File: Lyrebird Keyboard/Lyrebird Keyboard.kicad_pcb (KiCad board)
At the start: 4 copper layers, 220.1 x 160.3 mm, 99 parts, among them IC1 L7915CV, IC2 L78S15CV, IC3 MCP6022-E_SN, IC4 IR2113SPBF, IC5 IR2113SPBF, IC6 LM358DT, IC7 L7805ACD2T-TR, J1 WAV/ENV 4 (MIDI), J10 AC IN 2, J11 240V Out, J12 240 In, J13 Keys 1 to 14, J14 Keys 15 to 28, J15 Keys 29 to 33, J16 Keys 34 to 45, J17 Keys 46 to 59, J18 Keys 60 to 73, J19 Triangle Test, J2 WAV/ENV 3, J20 AMP Out, J21 SUB Out, J22 Square Test, J23 Bias Test Point 2, J24 Bias Test Point 1, J25 Pedals, J3 WAV/ENV 2, J4 WAV/ENV 1, J5 TONE SRC 4, J6 TONE SRC 3, J7 TONE SRC 2, J8 TONE SRC 1, J9 AC IN 1, Q1 BC848, Q2 BC848, Q3 IRFR2905ZTRPBF, Q4 IRFR2905ZTRPBF, Q5 IRFR2905ZTRPBF, Q6 IRFR2905ZTRPBF, U1 DF06S

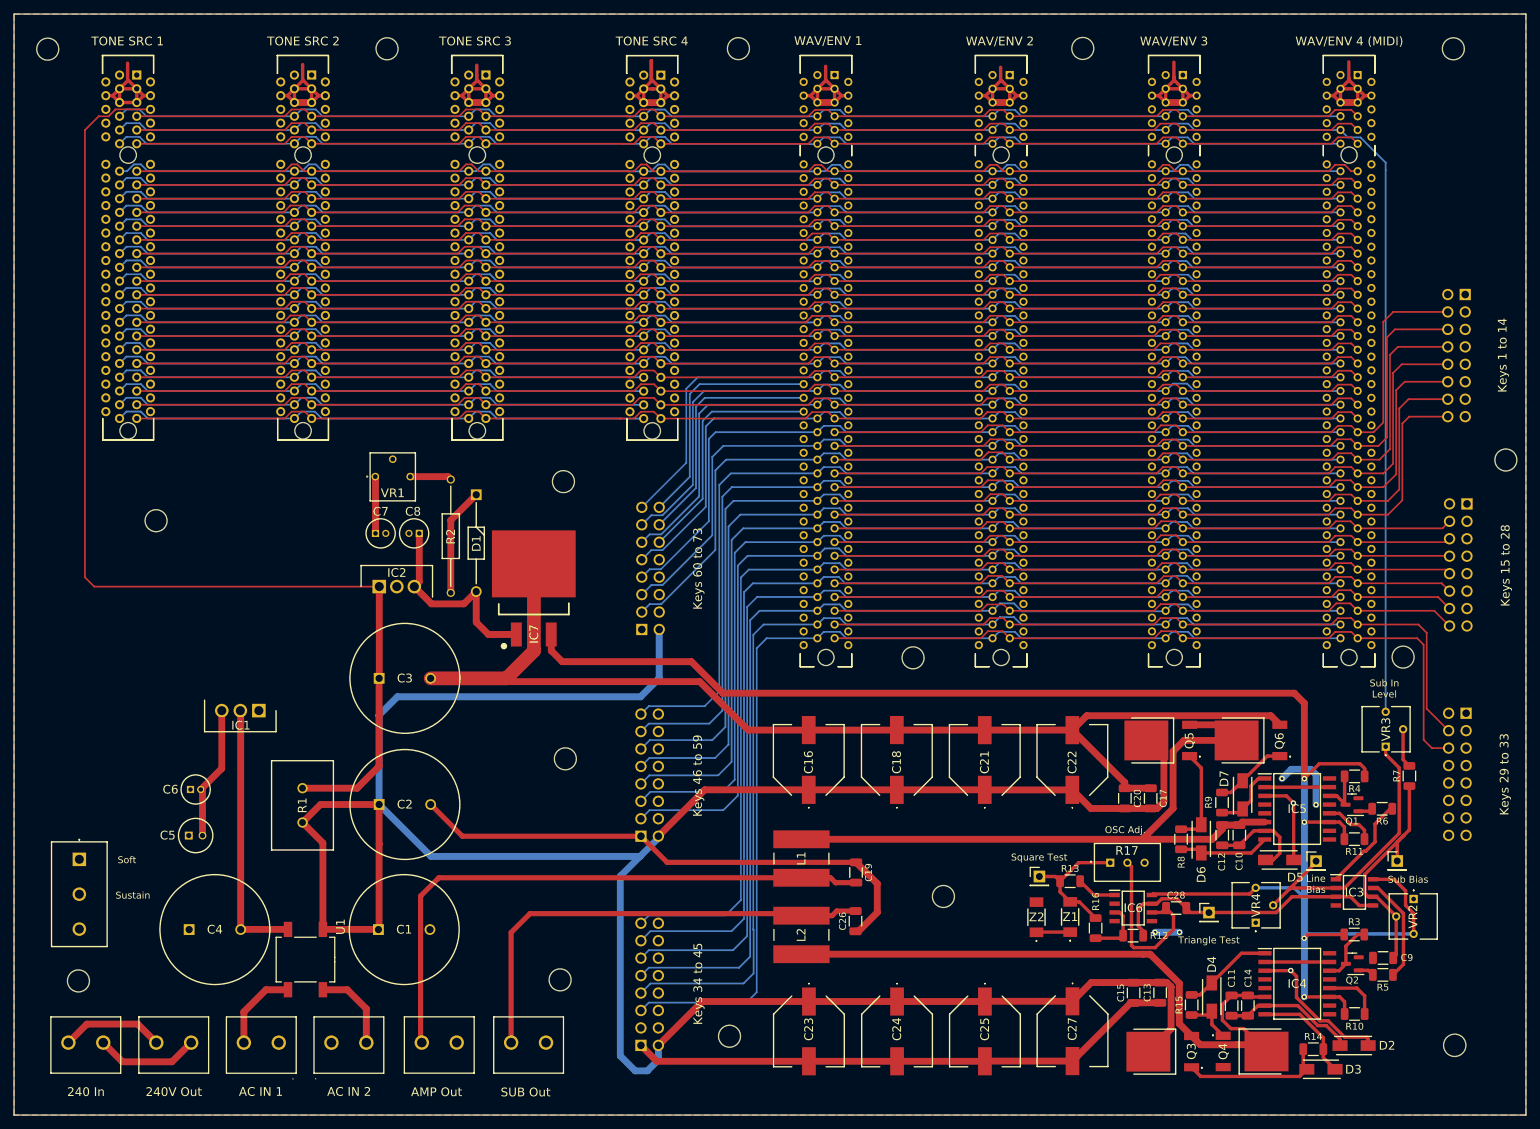
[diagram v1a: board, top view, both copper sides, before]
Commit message: Mainboard Changes
Adjusted mainboard, the longer PCI slots are now instrument slots not wave shaper slots, and slot 4 in the longer is also able to support midi implementation
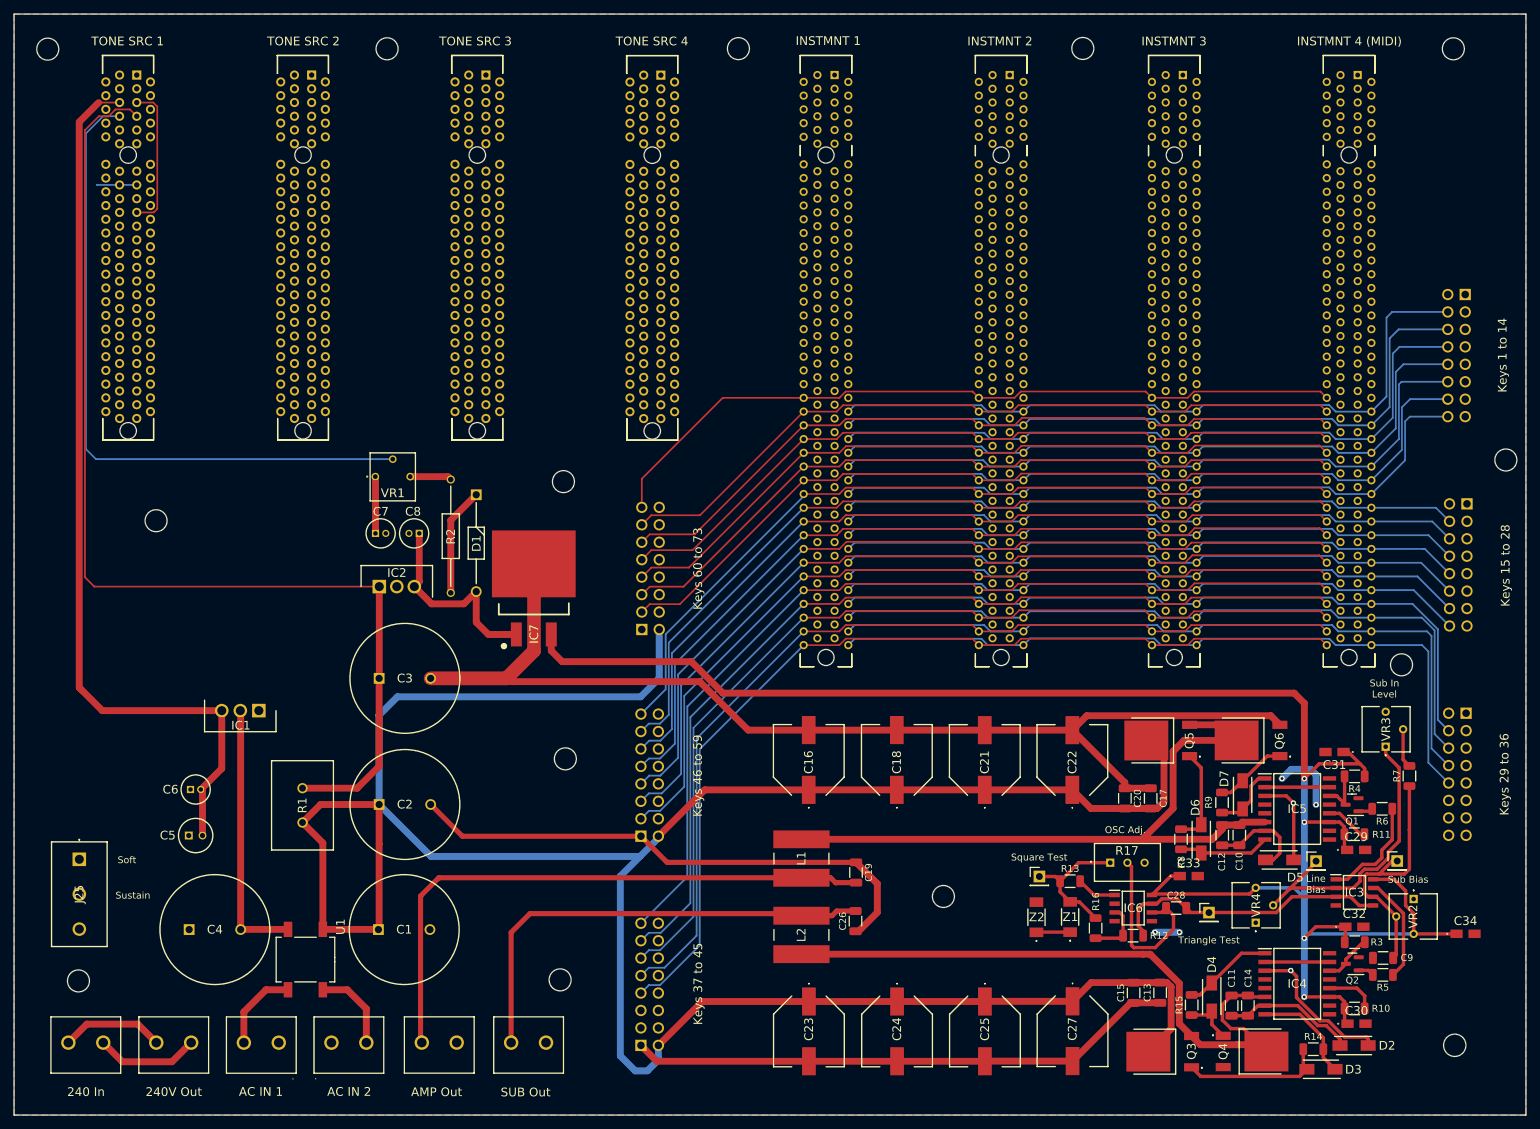
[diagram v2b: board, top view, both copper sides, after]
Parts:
- added C29: T491A225K016AT, SamacSys_Parts:T491A, F.Cu at (210.2, 135.7)
- added C30: T491A225K016AT, SamacSys_Parts:T491A, F.Cu at (210.2, 161.0)
- added C31: T491A225K016AT, SamacSys_Parts:T491A, F.Cu at (207.0, 121.5)
- added C32: T491A225K016AT, SamacSys_Parts:T491A, F.Cu at (209.9, 146.9)
- added C33: T491A225K016AT, SamacSys_Parts:T491A, F.Cu at (185.8, 139.5)
- added C34: T491A225K016AT, SamacSys_Parts:T491A, F.Cu at (226.1, 148.0)
- J1: value WAV/ENV 4 (MIDI) -> INSTMNT 4 (MIDI)
- J15: value Keys 29 to 33 -> Keys 29 to 36
- J16: value Keys 34 to 45 -> Keys 37 to 45
- J2: value WAV/ENV 3 -> INSTMNT 3
- J3: value WAV/ENV 2 -> INSTMNT 2
- J4: value WAV/ENV 1 -> INSTMNT 1
- moved R3 1.12 mm to (210.0, 149.2)
- moved R10 0.80 mm to (210.0, 158.8)
- moved R11 0.72 mm to (209.9, 133.5)
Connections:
- net A17S renamed EXP 7
- net B19S renamed TONE 8
- net B43S renamed TONE 7
- net C#69S renamed TONE 12
- net C20S renamed TONE 11
- net C44S renamed TONE 10
- net C68S renamed TONE 9
- net D#23S renamed EXP 4
- net D#47S renamed EXP 5
- net D#71S renamed EXP 6
- net D22S renamed EXP 12
- net D46S renamed EXP 11
- net E24S renamed EXP 1
- net E48S renamed EXP 2
- net E72S renamed EXP 3
- net EXP5 renamed SELECT 2
- net EXP7 renamed SELECT 3
- net F#26S renamed TONE 1
- net F#50S renamed TONE 2
- net F1S renamed TONE 3
- net F25S renamed TONE 4
- net F49S renamed TONE 5
- net F73S renamed TONE 6
- net G#28S renamed SELECT 6
- net G#52S renamed SELECT 7
- net G3S renamed SELECT 8
- J1 pad A1: +15V -> +30V
- J1 pad A10: G#40S -> GND
- J1 pad A12: G#64S -> GND
- J1 pad A14: G15S -> GND
- J1 pad A15: G27S -> +30V
- J1 pad A16: G39S -> GND
- J1 pad A17: G51S -> +15V
- J1 pad A18: G63S -> GND
- J1 pad A19: F#2S -> -15V
- J1 pad A2: -15V -> GND
- J1 pad A20: F#14S -> GND
- J1 pad A22: F#38S -> GND
- J1 pad A24: F#62S -> GND
- J1 pad A26: F13S -> GND
- J1 pad A28: F37S -> GND
- J1 pad A3: GND -> +15V
- J1 pad A30: F61S -> GND
- J1 pad A32: E12S -> GND
- J1 pad A34: E36S -> GND
- J1 pad A36: E60S -> GND
- J1 pad A38: D#11S -> GND
- J1 pad A40: D#35S -> GND
- J1 pad A42: D#59S -> GND
- J1 pad A44: A5S -> GND
- J1 pad A46: A29S -> GND
- J1 pad A47: A41S -> F1
- J1 pad A48: A53S -> F#2
- J1 pad A49: A65S -> G3
- J1 pad A5: GND -> -15V
- J1 pad A50: F1 -> G#4
- J1 pad A51: F#2 -> A5
- J1 pad A52: G3 -> A#6
- J1 pad A53: G#4 -> B7
- J1 pad A54: A5 -> C8
- J1 pad A55: A#6 -> C#9
- J1 pad A56: B7 -> D10
- J1 pad A57: C8 -> D#11
- J1 pad A58: C#9 -> E12
- J1 pad A59: D10 -> F13
- J1 pad A6: +VT -> GND
- J1 pad A60: D#11 -> F#14
- J1 pad A61: E12 -> G15
- J1 pad A62: F13 -> G#16
- J1 pad A63: F#14 -> A17
- J1 pad A64: G15 -> A#18
- J1 pad A65: G#16 -> B19
- J1 pad A66: A17 -> C20
- J1 pad A67: A#18 -> C#21
- J1 pad A68: B19 -> D22
- J1 pad A69: C20 -> D#23
- J1 pad A7: G#4S -> +VT
- J1 pad A70: C#21 -> E24
- J1 pad A71: D22 -> F25
- J1 pad A72: D#23 -> F#26
- J1 pad A73: E24 -> G27
- J1 pad A74: F25 -> G#28
- J1 pad A75: F#26 -> A29
- J1 pad A76: G27 -> A#30
- J1 pad A77: G#28 -> B31
- J1 pad A78: A29 -> C32
- J1 pad A79: A#30 -> C#33
- J1 pad A8: G#16S -> GND
- J1 pad A80: B31 -> D34
- J1 pad A81: C32 -> D#35
- J1 pad A82: C#33 -> E36
- J1 pad B1: +15V -> +30V
- J1 pad B10: EXP8 -> GND
- J1 pad B11: EXP9 -> SOFT
- J1 pad B12: EXP10 -> GND
- J1 pad B13: A#66S -> LINE OUT
- J1 pad B14: A#54S -> GND
- J1 pad B15: A#42S -> +30V
- J1 pad B16: A#30S -> GND
- J1 pad B17: A#18S -> +15V
- J1 pad B18: A#6S -> GND
- J1 pad B19: B67S -> -15V
- J1 pad B2: -15V -> GND
- J1 pad B20: B55S -> GND
- J1 pad B22: B31S -> GND
- J1 pad B24: B7S -> GND
- J1 pad B26: C56S -> GND
- J1 pad B28: C32S -> GND
- J1 pad B3: GND -> +15V
- J1 pad B30: C8S -> GND
- J1 pad B32: C#57S -> GND
- J1 pad B33: C#45S -> EXP8
- J1 pad B34: C#33S -> GND
- J1 pad B35: C#21S -> EXP9
- J1 pad B36: C#9S -> GND
- J1 pad B37: D70S -> EXP10
- J1 pad B38: D58S -> GND
- J1 pad B40: D34S -> GND
- J1 pad B42: D10S -> GND
- J1 pad B43: F73 -> EXP 13
- J1 pad B44: E72 -> GND
- J1 pad B45: D#71 -> SELECT 1
- J1 pad B46: D70 -> F73
- J1 pad B47: C#69 -> E72
- J1 pad B48: C68 -> D#71
- J1 pad B49: B67 -> D70
- J1 pad B5: GND -> -15V
- J1 pad B50: A#66 -> C#69
- J1 pad B51: A65 -> C68
- J1 pad B52: G#64 -> B67
- J1 pad B53: G63 -> A#66
- J1 pad B54: F#62 -> A65
- J1 pad B55: F61 -> G#64
- J1 pad B56: E60 -> G63
- J1 pad B57: D#59 -> F#62
- J1 pad B58: D58 -> F61
- J1 pad B59: C#57 -> E60
- J1 pad B6: +VED -> GND
- J1 pad B60: C56 -> D#59
- J1 pad B61: B55 -> D58
- J1 pad B62: A#54 -> C#57
- J1 pad B63: A53 -> C56
- J1 pad B64: G#52 -> B55
- J1 pad B65: G51 -> A#54
- J1 pad B66: F#50 -> A53
- J1 pad B67: F49 -> G#52
- J1 pad B68: E48 -> G51
- J1 pad B69: D#47 -> F#50
- J1 pad B7: SUSTAIN -> +VED
- J1 pad B70: D46 -> F49
- J1 pad B71: C#45 -> E48
- J1 pad B72: C44 -> D#47
- J1 pad B73: B43 -> D46
- J1 pad B74: A#42 -> C#45
- J1 pad B75: A41 -> C44
- J1 pad B76: G#40 -> B43
- J1 pad B77: G39 -> A#42
- J1 pad B78: F#38 -> A41
- J1 pad B79: F37 -> G#40
- J1 pad B8: SOFT -> GND
- J1 pad B80: E36 -> G39
- J1 pad B81: D#35 -> F#38
- J1 pad B82: D34 -> F37
- J1 pad B9: LINE OUT -> SUSTAIN
- J15 pad 10: unconnected-(J15-Pad10) -> E36
- J15 pad 8: unconnected-(J15-Pad8) -> D34
- J15 pad 9: unconnected-(J15-Pad9) -> D#35
- J16 pad 5: D#35 -> unconnected-(J16-Pad5)
- J16 pad 6: D34 -> unconnected-(J16-Pad6)
- J16 pad 8: E36 -> unconnected-(J16-Pad8)
- J2 pad A1: +15V -> +30V
- J2 pad A10: G#40S -> GND
- J2 pad A12: G#64S -> GND
- J2 pad A14: G15S -> GND
- J2 pad A15: G27S -> +30V
- J2 pad A16: G39S -> GND
- J2 pad A17: G51S -> +15V
- J2 pad A18: G63S -> GND
- J2 pad A19: F#2S -> -15V
- J2 pad A2: -15V -> GND
- J2 pad A20: F#14S -> GND
- J2 pad A22: F#38S -> GND
- J2 pad A24: F#62S -> GND
- J2 pad A26: F13S -> GND
- J2 pad A28: F37S -> GND
- J2 pad A3: GND -> +15V
- J2 pad A30: F61S -> GND
- J2 pad A32: E12S -> GND
- J2 pad A34: E36S -> GND
- J2 pad A36: E60S -> GND
- J2 pad A38: D#11S -> GND
- J2 pad A40: D#35S -> GND
- J2 pad A42: D#59S -> GND
- J2 pad A44: A5S -> GND
- J2 pad A46: A29S -> GND
- J2 pad A47: A41S -> F1
- J2 pad A48: A53S -> F#2
- J2 pad A49: A65S -> G3
- J2 pad A5: GND -> -15V
- J2 pad A50: F1 -> G#4
- J2 pad A51: F#2 -> A5
- J2 pad A52: G3 -> A#6
- J2 pad A53: G#4 -> B7
- J2 pad A54: A5 -> C8
- J2 pad A55: A#6 -> C#9
- J2 pad A56: B7 -> D10
- J2 pad A57: C8 -> D#11
- J2 pad A58: C#9 -> E12
- J2 pad A59: D10 -> F13
- J2 pad A6: +VT -> GND
- J2 pad A60: D#11 -> F#14
- J2 pad A61: E12 -> G15
- J2 pad A62: F13 -> G#16
- J2 pad A63: F#14 -> A17
- J2 pad A64: G15 -> A#18
- J2 pad A65: G#16 -> B19
- J2 pad A66: A17 -> C20
- J2 pad A67: A#18 -> C#21
- J2 pad A68: B19 -> D22
- J2 pad A69: C20 -> D#23
- J2 pad A7: G#4S -> +VT
- J2 pad A70: C#21 -> E24
- J2 pad A71: D22 -> F25
- J2 pad A72: D#23 -> F#26
- J2 pad A73: E24 -> G27
- J2 pad A74: F25 -> G#28
- J2 pad A75: F#26 -> A29
- J2 pad A76: G27 -> A#30
- J2 pad A77: G#28 -> B31
- J2 pad A78: A29 -> C32
- J2 pad A79: A#30 -> C#33
- J2 pad A8: G#16S -> GND
- J2 pad A80: B31 -> D34
- J2 pad A81: C32 -> D#35
- J2 pad A82: C#33 -> E36
- J2 pad B1: +15V -> +30V
- J2 pad B10: EXP8 -> GND
- J2 pad B11: EXP9 -> SOFT
- J2 pad B12: EXP10 -> GND
- J2 pad B13: A#66S -> LINE OUT
- J2 pad B14: A#54S -> GND
- J2 pad B15: A#42S -> +30V
- J2 pad B16: A#30S -> GND
- J2 pad B17: A#18S -> +15V
- J2 pad B18: A#6S -> GND
- J2 pad B19: B67S -> -15V
- J2 pad B2: -15V -> GND
- J2 pad B20: B55S -> GND
- J2 pad B22: B31S -> GND
- J2 pad B24: B7S -> GND
- J2 pad B26: C56S -> GND
- J2 pad B28: C32S -> GND
- J2 pad B3: GND -> +15V
- J2 pad B30: C8S -> GND
- J2 pad B32: C#57S -> GND
- J2 pad B33: C#45S -> EXP8
- J2 pad B34: C#33S -> GND
- J2 pad B35: C#21S -> EXP9
- J2 pad B36: C#9S -> GND
- J2 pad B37: D70S -> EXP10
- J2 pad B38: D58S -> GND
- J2 pad B40: D34S -> GND
- J2 pad B42: D10S -> GND
- J2 pad B43: F73 -> EXP 13
- J2 pad B44: E72 -> GND
- J2 pad B45: D#71 -> SELECT 1
- J2 pad B46: D70 -> F73
- J2 pad B47: C#69 -> E72
- J2 pad B48: C68 -> D#71
- J2 pad B49: B67 -> D70
- J2 pad B5: GND -> -15V
- J2 pad B50: A#66 -> C#69
- J2 pad B51: A65 -> C68
- J2 pad B52: G#64 -> B67
- J2 pad B53: G63 -> A#66
- J2 pad B54: F#62 -> A65
- J2 pad B55: F61 -> G#64
- J2 pad B56: E60 -> G63
- J2 pad B57: D#59 -> F#62
- J2 pad B58: D58 -> F61
- J2 pad B59: C#57 -> E60
- J2 pad B6: +VED -> GND
- J2 pad B60: C56 -> D#59
- J2 pad B61: B55 -> D58
- J2 pad B62: A#54 -> C#57
- J2 pad B63: A53 -> C56
- J2 pad B64: G#52 -> B55
- J2 pad B65: G51 -> A#54
- J2 pad B66: F#50 -> A53
- J2 pad B67: F49 -> G#52
- J2 pad B68: E48 -> G51
- J2 pad B69: D#47 -> F#50
- J2 pad B7: SUSTAIN -> +VED
- J2 pad B70: D46 -> F49
- J2 pad B71: C#45 -> E48
- J2 pad B72: C44 -> D#47
- J2 pad B73: B43 -> D46
- J2 pad B74: A#42 -> C#45
- J2 pad B75: A41 -> C44
- J2 pad B76: G#40 -> B43
- J2 pad B77: G39 -> A#42
- J2 pad B78: F#38 -> A41
- J2 pad B79: F37 -> G#40
- J2 pad B8: SOFT -> GND
- J2 pad B80: E36 -> G39
- J2 pad B81: D#35 -> F#38
- J2 pad B82: D34 -> F37
- J2 pad B9: LINE OUT -> SUSTAIN
- J3 pad A1: +15V -> +30V
- J3 pad A10: G#40S -> GND
- J3 pad A12: G#64S -> GND
- J3 pad A14: G15S -> GND
- J3 pad A15: G27S -> +30V
- J3 pad A16: G39S -> GND
- J3 pad A17: G51S -> +15V
- J3 pad A18: G63S -> GND
- J3 pad A19: F#2S -> -15V
- J3 pad A2: -15V -> GND
- J3 pad A20: F#14S -> GND
- J3 pad A22: F#38S -> GND
- J3 pad A24: F#62S -> GND
- J3 pad A26: F13S -> GND
- J3 pad A28: F37S -> GND
- J3 pad A3: GND -> +15V
- J3 pad A30: F61S -> GND
- J3 pad A32: E12S -> GND
- J3 pad A34: E36S -> GND
- J3 pad A36: E60S -> GND
- J3 pad A38: D#11S -> GND
- J3 pad A40: D#35S -> GND
- J3 pad A42: D#59S -> GND
- J3 pad A44: A5S -> GND
- J3 pad A46: A29S -> GND
- J3 pad A47: A41S -> F1
- J3 pad A48: A53S -> F#2
- J3 pad A49: A65S -> G3
- J3 pad A5: GND -> -15V
- J3 pad A50: F1 -> G#4
- J3 pad A51: F#2 -> A5
- J3 pad A52: G3 -> A#6
- J3 pad A53: G#4 -> B7
- J3 pad A54: A5 -> C8
- J3 pad A55: A#6 -> C#9
- J3 pad A56: B7 -> D10
- J3 pad A57: C8 -> D#11
- J3 pad A58: C#9 -> E12
- J3 pad A59: D10 -> F13
- J3 pad A6: +VT -> GND
- J3 pad A60: D#11 -> F#14
- J3 pad A61: E12 -> G15
- J3 pad A62: F13 -> G#16
- J3 pad A63: F#14 -> A17
- J3 pad A64: G15 -> A#18
- J3 pad A65: G#16 -> B19
- J3 pad A66: A17 -> C20
- J3 pad A67: A#18 -> C#21
- J3 pad A68: B19 -> D22
- J3 pad A69: C20 -> D#23
- J3 pad A7: G#4S -> +VT
- J3 pad A70: C#21 -> E24
- J3 pad A71: D22 -> F25
- J3 pad A72: D#23 -> F#26
- J3 pad A73: E24 -> G27
- J3 pad A74: F25 -> G#28
- J3 pad A75: F#26 -> A29
- J3 pad A76: G27 -> A#30
- J3 pad A77: G#28 -> B31
- J3 pad A78: A29 -> C32
- J3 pad A79: A#30 -> C#33
- J3 pad A8: G#16S -> GND
- J3 pad A80: B31 -> D34
- J3 pad A81: C32 -> D#35
- J3 pad A82: C#33 -> E36
- J3 pad B1: +15V -> +30V
- J3 pad B10: EXP8 -> GND
- J3 pad B11: EXP9 -> SOFT
- J3 pad B12: EXP10 -> GND
- J3 pad B13: A#66S -> LINE OUT
- J3 pad B14: A#54S -> GND
- J3 pad B15: A#42S -> +30V
- J3 pad B16: A#30S -> GND
- J3 pad B17: A#18S -> +15V
- J3 pad B18: A#6S -> GND
- J3 pad B19: B67S -> -15V
- J3 pad B2: -15V -> GND
- J3 pad B20: B55S -> GND
- J3 pad B22: B31S -> GND
- J3 pad B24: B7S -> GND
- J3 pad B26: C56S -> GND
- J3 pad B28: C32S -> GND
- J3 pad B3: GND -> +15V
- J3 pad B30: C8S -> GND
- J3 pad B32: C#57S -> GND
- J3 pad B33: C#45S -> EXP8
- J3 pad B34: C#33S -> GND
- J3 pad B35: C#21S -> EXP9
- J3 pad B36: C#9S -> GND
- J3 pad B37: D70S -> EXP10
- J3 pad B38: D58S -> GND
- J3 pad B40: D34S -> GND
- J3 pad B42: D10S -> GND
- J3 pad B43: F73 -> EXP 13
- J3 pad B44: E72 -> GND
- J3 pad B45: D#71 -> SELECT 1
- J3 pad B46: D70 -> F73
- J3 pad B47: C#69 -> E72
- J3 pad B48: C68 -> D#71
- J3 pad B49: B67 -> D70
- J3 pad B5: GND -> -15V
- J3 pad B50: A#66 -> C#69
- J3 pad B51: A65 -> C68
- J3 pad B52: G#64 -> B67
- J3 pad B53: G63 -> A#66
- J3 pad B54: F#62 -> A65
- J3 pad B55: F61 -> G#64
- J3 pad B56: E60 -> G63
- J3 pad B57: D#59 -> F#62
- J3 pad B58: D58 -> F61
- J3 pad B59: C#57 -> E60
- J3 pad B6: +VED -> GND
- J3 pad B60: C56 -> D#59
- J3 pad B61: B55 -> D58
- J3 pad B62: A#54 -> C#57
- J3 pad B63: A53 -> C56
- J3 pad B64: G#52 -> B55
- J3 pad B65: G51 -> A#54
- J3 pad B66: F#50 -> A53
- J3 pad B67: F49 -> G#52
- J3 pad B68: E48 -> G51
- J3 pad B69: D#47 -> F#50
- J3 pad B7: SUSTAIN -> +VED
- J3 pad B70: D46 -> F49
- J3 pad B71: C#45 -> E48
- J3 pad B72: C44 -> D#47
- J3 pad B73: B43 -> D46
- J3 pad B74: A#42 -> C#45
- J3 pad B75: A41 -> C44
- J3 pad B76: G#40 -> B43
- J3 pad B77: G39 -> A#42
- J3 pad B78: F#38 -> A41
- J3 pad B79: F37 -> G#40
- J3 pad B8: SOFT -> GND
- J3 pad B80: E36 -> G39
- J3 pad B81: D#35 -> F#38
- J3 pad B82: D34 -> F37
- J3 pad B9: LINE OUT -> SUSTAIN
- J4 pad A1: +15V -> +30V
- J4 pad A10: G#40S -> GND
- J4 pad A12: G#64S -> GND
- J4 pad A14: G15S -> GND
- J4 pad A15: G27S -> +30V
- J4 pad A16: G39S -> GND
- J4 pad A17: G51S -> +15V
- J4 pad A18: G63S -> GND
- J4 pad A19: F#2S -> -15V
- J4 pad A2: -15V -> GND
- J4 pad A20: F#14S -> GND
- J4 pad A22: F#38S -> GND
- J4 pad A24: F#62S -> GND
- J4 pad A26: F13S -> GND
- J4 pad A28: F37S -> GND
- J4 pad A3: GND -> +15V
- J4 pad A30: F61S -> GND
- J4 pad A32: E12S -> GND
- J4 pad A34: E36S -> GND
- J4 pad A36: E60S -> GND
- J4 pad A38: D#11S -> GND
- J4 pad A40: D#35S -> GND
- J4 pad A42: D#59S -> GND
- J4 pad A44: A5S -> GND
- J4 pad A46: A29S -> GND
- J4 pad A47: A41S -> F1
- J4 pad A48: A53S -> F#2
- J4 pad A49: A65S -> G3
- J4 pad A5: GND -> -15V
- J4 pad A50: F1 -> G#4
- J4 pad A51: F#2 -> A5
- J4 pad A52: G3 -> A#6
- J4 pad A53: G#4 -> B7
- J4 pad A54: A5 -> C8
- J4 pad A55: A#6 -> C#9
- J4 pad A56: B7 -> D10
- J4 pad A57: C8 -> D#11
- J4 pad A58: C#9 -> E12
- J4 pad A59: D10 -> F13
- J4 pad A6: +VT -> GND
- J4 pad A60: D#11 -> F#14
- J4 pad A61: E12 -> G15
- J4 pad A62: F13 -> G#16
- J4 pad A63: F#14 -> A17
- J4 pad A64: G15 -> A#18
- J4 pad A65: G#16 -> B19
- J4 pad A66: A17 -> C20
- J4 pad A67: A#18 -> C#21
- J4 pad A68: B19 -> D22
- J4 pad A69: C20 -> D#23
- J4 pad A7: G#4S -> +VT
- J4 pad A70: C#21 -> E24
- J4 pad A71: D22 -> F25
- J4 pad A72: D#23 -> F#26
- J4 pad A73: E24 -> G27
- J4 pad A74: F25 -> G#28
- J4 pad A75: F#26 -> A29
- J4 pad A76: G27 -> A#30
- J4 pad A77: G#28 -> B31
- J4 pad A78: A29 -> C32
- J4 pad A79: A#30 -> C#33
- J4 pad A8: G#16S -> GND
- J4 pad A80: B31 -> D34
- J4 pad A81: C32 -> D#35
- J4 pad A82: C#33 -> E36
- J4 pad B1: +15V -> +30V
- J4 pad B10: EXP8 -> GND
- J4 pad B11: EXP9 -> SOFT
- J4 pad B12: EXP10 -> GND
- J4 pad B13: A#66S -> LINE OUT
- J4 pad B14: A#54S -> GND
- J4 pad B15: A#42S -> +30V
- J4 pad B16: A#30S -> GND
- J4 pad B17: A#18S -> +15V
- J4 pad B18: A#6S -> GND
- J4 pad B19: B67S -> -15V
- J4 pad B2: -15V -> GND
- J4 pad B20: B55S -> GND
- J4 pad B22: B31S -> GND
- J4 pad B24: B7S -> GND
- J4 pad B26: C56S -> GND
- J4 pad B28: C32S -> GND
- J4 pad B3: GND -> +15V
- J4 pad B30: C8S -> GND
- J4 pad B32: C#57S -> GND
- J4 pad B33: C#45S -> EXP8
- J4 pad B34: C#33S -> GND
- J4 pad B35: C#21S -> EXP9
- J4 pad B36: C#9S -> GND
- J4 pad B37: D70S -> EXP10
- J4 pad B38: D58S -> GND
- J4 pad B40: D34S -> GND
- J4 pad B42: D10S -> GND
- J4 pad B43: F73 -> EXP 13
- J4 pad B44: E72 -> GND
- J4 pad B45: D#71 -> SELECT 1
- J4 pad B46: D70 -> F73
- J4 pad B47: C#69 -> E72
- J4 pad B48: C68 -> D#71
- J4 pad B49: B67 -> D70
- J4 pad B5: GND -> -15V
- J4 pad B50: A#66 -> C#69
- J4 pad B51: A65 -> C68
- J4 pad B52: G#64 -> B67
- J4 pad B53: G63 -> A#66
- J4 pad B54: F#62 -> A65
- J4 pad B55: F61 -> G#64
- J4 pad B56: E60 -> G63
- J4 pad B57: D#59 -> F#62
- J4 pad B58: D58 -> F61
- J4 pad B59: C#57 -> E60
- J4 pad B6: +VED -> GND
- J4 pad B60: C56 -> D#59
- J4 pad B61: B55 -> D58
- J4 pad B62: A#54 -> C#57
- J4 pad B63: A53 -> C56
- J4 pad B64: G#52 -> B55
- J4 pad B65: G51 -> A#54
- J4 pad B66: F#50 -> A53
- J4 pad B67: F49 -> G#52
- J4 pad B68: E48 -> G51
- J4 pad B69: D#47 -> F#50
- J4 pad B7: SUSTAIN -> +VED
- J4 pad B70: D46 -> F49
- J4 pad B71: C#45 -> E48
- J4 pad B72: C44 -> D#47
- J4 pad B73: B43 -> D46
- J4 pad B74: A#42 -> C#45
- J4 pad B75: A41 -> C44
- J4 pad B76: G#40 -> B43
- J4 pad B77: G39 -> A#42
- J4 pad B78: F#38 -> A41
- J4 pad B79: F37 -> G#40
- J4 pad B8: SOFT -> GND
- J4 pad B80: E36 -> G39
- J4 pad B81: D#35 -> F#38
- J4 pad B82: D34 -> F37
- J4 pad B9: LINE OUT -> SUSTAIN
- J5 pad A1: +15V -> +30V
- J5 pad A10: G#40S -> GND
- J5 pad A12: G#64S -> GND
- J5 pad A14: G15S -> GND
- J5 pad A15: G27S -> +30V
- J5 pad A16: G39S -> GND
- J5 pad A17: G51S -> +15V
- J5 pad A18: G63S -> GND
- J5 pad A19: F#2S -> -15V
- J5 pad A2: -15V -> GND
- J5 pad A20: F#14S -> GND
- J5 pad A22: F#38S -> GND
- J5 pad A24: F#62S -> GND
- J5 pad A26: F13S -> GND
- J5 pad A28: F37S -> GND
- J5 pad A3: GND -> +15V
- J5 pad A30: F61S -> GND
- J5 pad A32: E12S -> GND
- J5 pad A34: E36S -> GND
- J5 pad A36: E60S -> GND
- J5 pad A38: D#11S -> GND
- J5 pad A40: D#35S -> GND
- J5 pad A42: D#59S -> GND
- J5 pad A44: A5S -> GND
- J5 pad A46: A29S -> GND
- J5 pad A47: A41S -> SELECT 4
- J5 pad A48: A53S -> GND
- J5 pad A49: A65S -> SELECT 5
- J5 pad A5: GND -> -15V
- J5 pad A6: +VT -> GND
- J5 pad A7: G#4S -> +VT
- J5 pad A8: G#16S -> GND
- J5 pad B1: +15V -> +30V
- J5 pad B10: EXP8 -> GND
- J5 pad B11: EXP9 -> SOFT
- J5 pad B12: EXP10 -> GND
- J5 pad B13: A#66S -> LINE OUT
- J5 pad B14: A#54S -> GND
- J5 pad B15: A#42S -> +30V
- J5 pad B16: A#30S -> GND
- J5 pad B17: A#18S -> +15V
- J5 pad B18: A#6S -> GND
- J5 pad B19: B67S -> -15V
- J5 pad B2: -15V -> GND
- J5 pad B20: B55S -> GND
- J5 pad B22: B31S -> GND
- J5 pad B24: B7S -> GND
- J5 pad B26: C56S -> GND
- J5 pad B28: C32S -> GND
- J5 pad B3: GND -> +15V
- J5 pad B30: C8S -> GND
- J5 pad B32: C#57S -> GND
- J5 pad B33: C#45S -> EXP8
- J5 pad B34: C#33S -> GND
- J5 pad B35: C#21S -> EXP9
- J5 pad B36: C#9S -> GND
- J5 pad B37: D70S -> EXP10
- J5 pad B38: D58S -> GND
- J5 pad B40: D34S -> GND
- J5 pad B42: D10S -> GND
- J5 pad B43: EXP1 -> EXP 13
- J5 pad B44: EXP2 -> GND
- J5 pad B45: EXP3 -> SELECT 1
- J5 pad B46: EXP4 -> GND
- J5 pad B48: EXP6 -> GND
- J5 pad B5: GND -> -15V
- J5 pad B6: +VED -> GND
- J5 pad B7: SUSTAIN -> +VED
- J5 pad B8: SOFT -> GND
- J5 pad B9: LINE OUT -> SUSTAIN
- J6 pad A1: +15V -> +30V
- J6 pad A10: G#40S -> GND
- J6 pad A12: G#64S -> GND
- J6 pad A14: G15S -> GND
- J6 pad A15: G27S -> +30V
- J6 pad A16: G39S -> GND
- J6 pad A17: G51S -> +15V
- J6 pad A18: G63S -> GND
- J6 pad A19: F#2S -> -15V
- J6 pad A2: -15V -> GND
- J6 pad A20: F#14S -> GND
- J6 pad A22: F#38S -> GND
- J6 pad A24: F#62S -> GND
- J6 pad A26: F13S -> GND
- J6 pad A28: F37S -> GND
- J6 pad A3: GND -> +15V
- J6 pad A30: F61S -> GND
- J6 pad A32: E12S -> GND
- J6 pad A34: E36S -> GND
- J6 pad A36: E60S -> GND
- J6 pad A38: D#11S -> GND
- J6 pad A40: D#35S -> GND
- J6 pad A42: D#59S -> GND
- J6 pad A44: A5S -> GND
- J6 pad A46: A29S -> GND
- J6 pad A47: A41S -> SELECT 4
- J6 pad A48: A53S -> GND
- J6 pad A49: A65S -> SELECT 5
- J6 pad A5: GND -> -15V
- J6 pad A6: +VT -> GND
- J6 pad A7: G#4S -> +VT
- J6 pad A8: G#16S -> GND
- J6 pad B1: +15V -> +30V
- J6 pad B10: EXP8 -> GND
- J6 pad B11: EXP9 -> SOFT
- J6 pad B12: EXP10 -> GND
- J6 pad B13: A#66S -> LINE OUT
- J6 pad B14: A#54S -> GND
- J6 pad B15: A#42S -> +30V
- J6 pad B16: A#30S -> GND
- J6 pad B17: A#18S -> +15V
- J6 pad B18: A#6S -> GND
- J6 pad B19: B67S -> -15V
- J6 pad B2: -15V -> GND
- J6 pad B20: B55S -> GND
- J6 pad B22: B31S -> GND
- J6 pad B24: B7S -> GND
- J6 pad B26: C56S -> GND
- J6 pad B28: C32S -> GND
- J6 pad B3: GND -> +15V
- J6 pad B30: C8S -> GND
- J6 pad B32: C#57S -> GND
- J6 pad B33: C#45S -> EXP8
- J6 pad B34: C#33S -> GND
- J6 pad B35: C#21S -> EXP9
- J6 pad B36: C#9S -> GND
- J6 pad B37: D70S -> EXP10
- J6 pad B38: D58S -> GND
- J6 pad B40: D34S -> GND
- J6 pad B42: D10S -> GND
- J6 pad B43: EXP1 -> EXP 13
- J6 pad B44: EXP2 -> GND
- J6 pad B45: EXP3 -> SELECT 1
- J6 pad B46: EXP4 -> GND
- J6 pad B48: EXP6 -> GND
- J6 pad B5: GND -> -15V
- J6 pad B6: +VED -> GND
- J6 pad B7: SUSTAIN -> +VED
- J6 pad B8: SOFT -> GND
- J6 pad B9: LINE OUT -> SUSTAIN
- J7 pad A1: +15V -> +30V
- J7 pad A10: G#40S -> GND
- J7 pad A12: G#64S -> GND
- J7 pad A14: G15S -> GND
- J7 pad A15: G27S -> +30V
- J7 pad A16: G39S -> GND
- J7 pad A17: G51S -> +15V
- J7 pad A18: G63S -> GND
- J7 pad A19: F#2S -> -15V
- J7 pad A2: -15V -> GND
- J7 pad A20: F#14S -> GND
- J7 pad A22: F#38S -> GND
- J7 pad A24: F#62S -> GND
- J7 pad A26: F13S -> GND
- J7 pad A28: F37S -> GND
- J7 pad A3: GND -> +15V
- J7 pad A30: F61S -> GND
- J7 pad A32: E12S -> GND
- J7 pad A34: E36S -> GND
- J7 pad A36: E60S -> GND
- J7 pad A38: D#11S -> GND
- J7 pad A40: D#35S -> GND
- J7 pad A42: D#59S -> GND
- J7 pad A44: A5S -> GND
- J7 pad A46: A29S -> GND
- J7 pad A47: A41S -> SELECT 4
- J7 pad A48: A53S -> GND
- J7 pad A49: A65S -> SELECT 5
- J7 pad A5: GND -> -15V
- J7 pad A6: +VT -> GND
- J7 pad A7: G#4S -> +VT
- J7 pad A8: G#16S -> GND
- J7 pad B1: +15V -> +30V
- J7 pad B10: EXP8 -> GND
- J7 pad B11: EXP9 -> SOFT
- J7 pad B12: EXP10 -> GND
- J7 pad B13: A#66S -> LINE OUT
- J7 pad B14: A#54S -> GND
- J7 pad B15: A#42S -> +30V
- J7 pad B16: A#30S -> GND
- J7 pad B17: A#18S -> +15V
- J7 pad B18: A#6S -> GND
- J7 pad B19: B67S -> -15V
- J7 pad B2: -15V -> GND
- J7 pad B20: B55S -> GND
- J7 pad B22: B31S -> GND
- J7 pad B24: B7S -> GND
- J7 pad B26: C56S -> GND
- J7 pad B28: C32S -> GND
- J7 pad B3: GND -> +15V
- J7 pad B30: C8S -> GND
- J7 pad B32: C#57S -> GND
- J7 pad B33: C#45S -> EXP8
- J7 pad B34: C#33S -> GND
- J7 pad B35: C#21S -> EXP9
- J7 pad B36: C#9S -> GND
- J7 pad B37: D70S -> EXP10
- J7 pad B38: D58S -> GND
- J7 pad B40: D34S -> GND
- J7 pad B42: D10S -> GND
- J7 pad B43: EXP1 -> EXP 13
- J7 pad B44: EXP2 -> GND
- J7 pad B45: EXP3 -> SELECT 1
- J7 pad B46: EXP4 -> GND
- J7 pad B48: EXP6 -> GND
- J7 pad B5: GND -> -15V
- J7 pad B6: +VED -> GND
- J7 pad B7: SUSTAIN -> +VED
- J7 pad B8: SOFT -> GND
- J7 pad B9: LINE OUT -> SUSTAIN
- J8 pad A1: +15V -> +30V
- J8 pad A10: G#40S -> GND
- J8 pad A12: G#64S -> GND
- J8 pad A14: G15S -> GND
- J8 pad A15: G27S -> +30V
- J8 pad A16: G39S -> GND
- J8 pad A17: G51S -> +15V
- J8 pad A18: G63S -> GND
- J8 pad A19: F#2S -> -15V
- J8 pad A2: -15V -> GND
- J8 pad A20: F#14S -> GND
- J8 pad A22: F#38S -> GND
- J8 pad A24: F#62S -> GND
- J8 pad A26: F13S -> GND
- J8 pad A28: F37S -> GND
- J8 pad A3: GND -> +15V
- J8 pad A30: F61S -> GND
- J8 pad A32: E12S -> GND
- J8 pad A34: E36S -> GND
- J8 pad A36: E60S -> GND
- J8 pad A38: D#11S -> GND
- J8 pad A40: D#35S -> GND
- J8 pad A42: D#59S -> GND
- J8 pad A44: A5S -> GND
- J8 pad A46: A29S -> GND
- J8 pad A47: A41S -> SELECT 4
- J8 pad A48: A53S -> GND
- J8 pad A49: A65S -> SELECT 5
- J8 pad A5: GND -> -15V
- J8 pad A6: +VT -> GND
- J8 pad A7: G#4S -> +VT
- J8 pad A8: G#16S -> GND
- J8 pad B1: +15V -> +30V
- J8 pad B10: EXP8 -> GND
- J8 pad B11: EXP9 -> SOFT
- J8 pad B12: EXP10 -> GND
- J8 pad B13: A#66S -> LINE OUT
- J8 pad B14: A#54S -> GND
- J8 pad B15: A#42S -> +30V
- J8 pad B16: A#30S -> GND
- J8 pad B17: A#18S -> +15V
- J8 pad B18: A#6S -> GND
- J8 pad B19: B67S -> -15V
- J8 pad B2: -15V -> GND
- J8 pad B20: B55S -> GND
- J8 pad B22: B31S -> GND
- J8 pad B24: B7S -> GND
- J8 pad B26: C56S -> GND
- J8 pad B28: C32S -> GND
- J8 pad B3: GND -> +15V
- J8 pad B30: C8S -> GND
- J8 pad B32: C#57S -> GND
- J8 pad B33: C#45S -> EXP8
- J8 pad B34: C#33S -> GND
- J8 pad B35: C#21S -> EXP9
- J8 pad B36: C#9S -> GND
- J8 pad B37: D70S -> EXP10
- J8 pad B38: D58S -> GND
- J8 pad B40: D34S -> GND
- J8 pad B42: D10S -> GND
- J8 pad B43: EXP1 -> EXP 13
- J8 pad B44: EXP2 -> GND
- J8 pad B45: EXP3 -> SELECT 1
- J8 pad B46: EXP4 -> GND
- J8 pad B48: EXP6 -> GND
- J8 pad B5: GND -> -15V
- J8 pad B6: +VED -> GND
- J8 pad B7: SUSTAIN -> +VED
- J8 pad B8: SOFT -> GND
- J8 pad B9: LINE OUT -> SUSTAIN
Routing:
- net +15V: track 266.9 -> 756.5 mm
- net -15V: track 71.6 -> 513.0 mm
- net +30V: track 380.7 -> 587.8 mm
- net A53S: track 204.3 -> 0.00 mm
- net A5S: track 191.4 -> 0.00 mm
- net F37S: track 191.3 -> 0.00 mm
- net E36S: track 191.3 -> 0.00 mm
- net G#64S: track 191.2 -> 0.00 mm
- net F13S: track 191.1 -> 0.00 mm
- net F61S: track 191.1 -> 0.00 mm
- net F#14S: track 191.1 -> 0.00 mm
- net D#35S: track 191.1 -> 0.00 mm
- net F#38S: track 191.1 -> 0.00 mm
- net G63S: track 191.1 -> 0.00 mm
- net A29S: track 191.1 -> 0.00 mm
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- removed copper zone on In1.Cu, net +15V
- removed copper zone on In2.Cu, net -15V
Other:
- outline, holes or cut-outs redrawn

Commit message: Piano Board Layout
Started doing circuit that creates the piano sound.
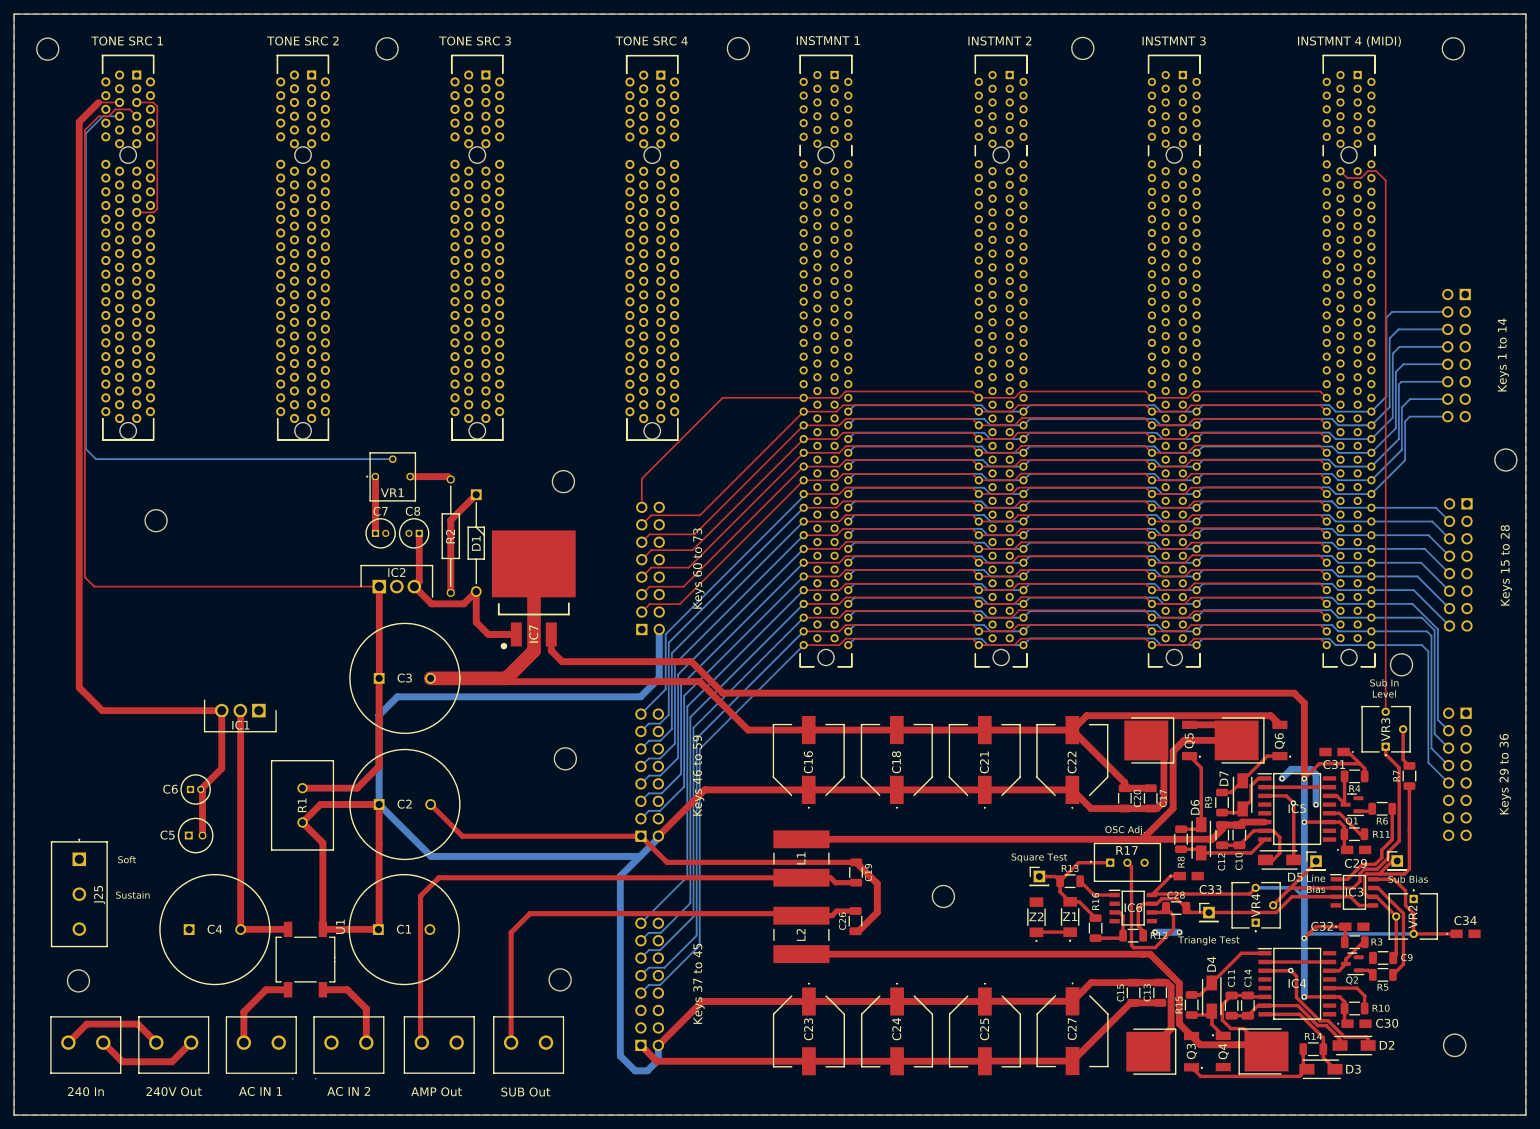
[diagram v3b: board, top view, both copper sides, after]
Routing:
- net +30V: track 587.8 -> 1044.3 mm
- net LINE OUT: track 183.4 -> 268.7 mm
- net +15V: track 756.5 -> 755.6 mm
- added copper zone on B.Cu, net GND
- removed copper zone on B.Cu, net +30V
